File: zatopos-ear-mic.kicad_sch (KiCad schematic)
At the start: 20 parts, among them J2 Conn_01x06_Socket, U1 NJU7043, U2 MCP3002

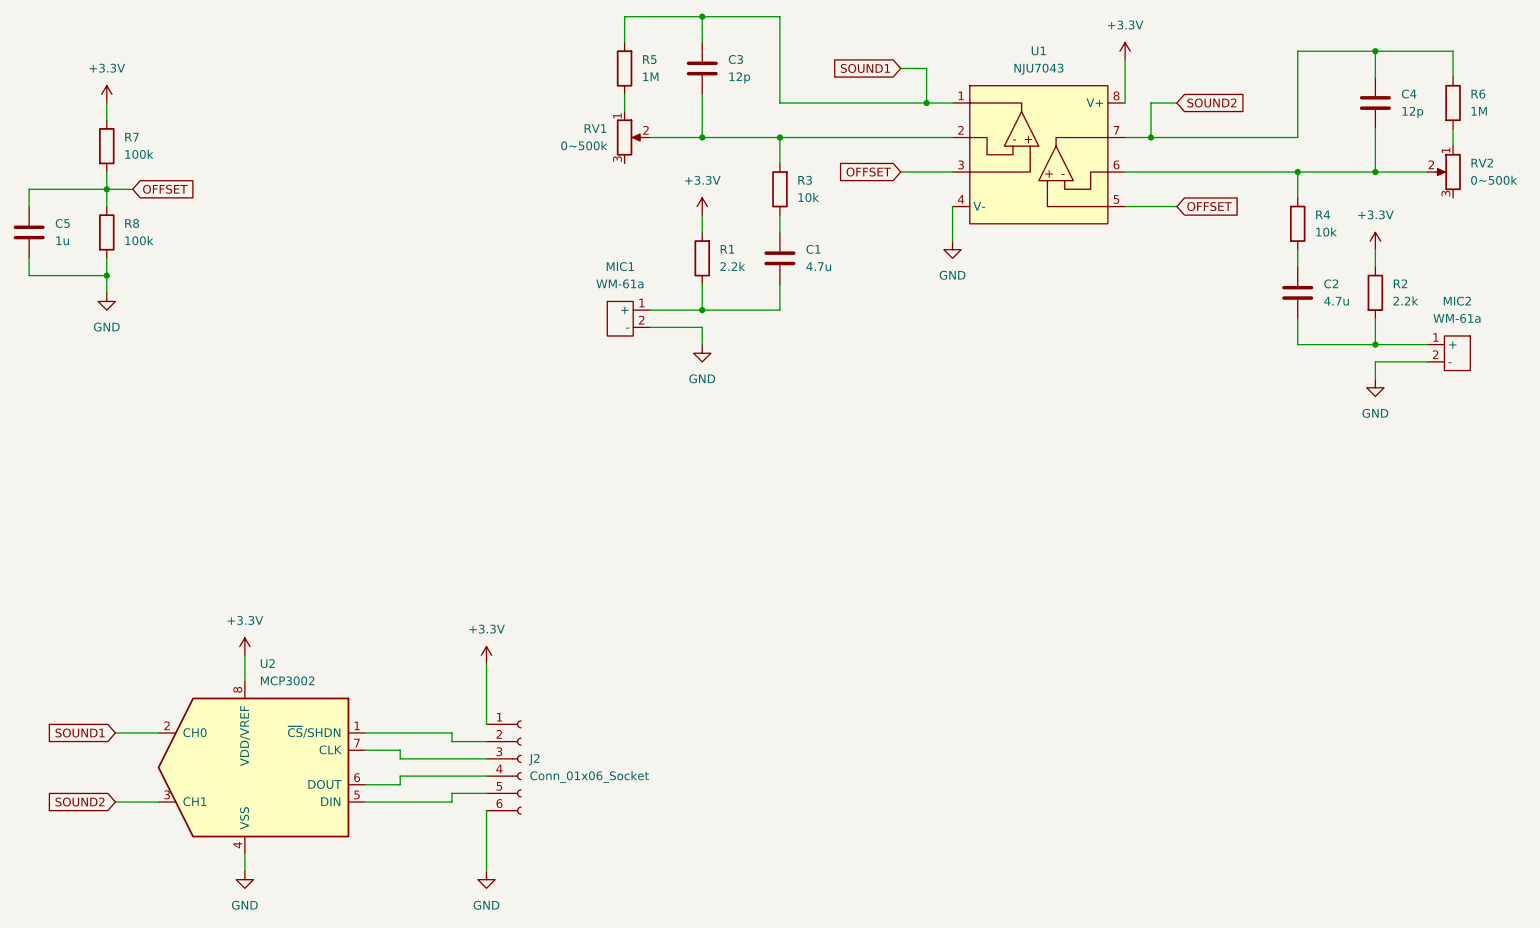
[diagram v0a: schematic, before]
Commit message: Fix ERC errors
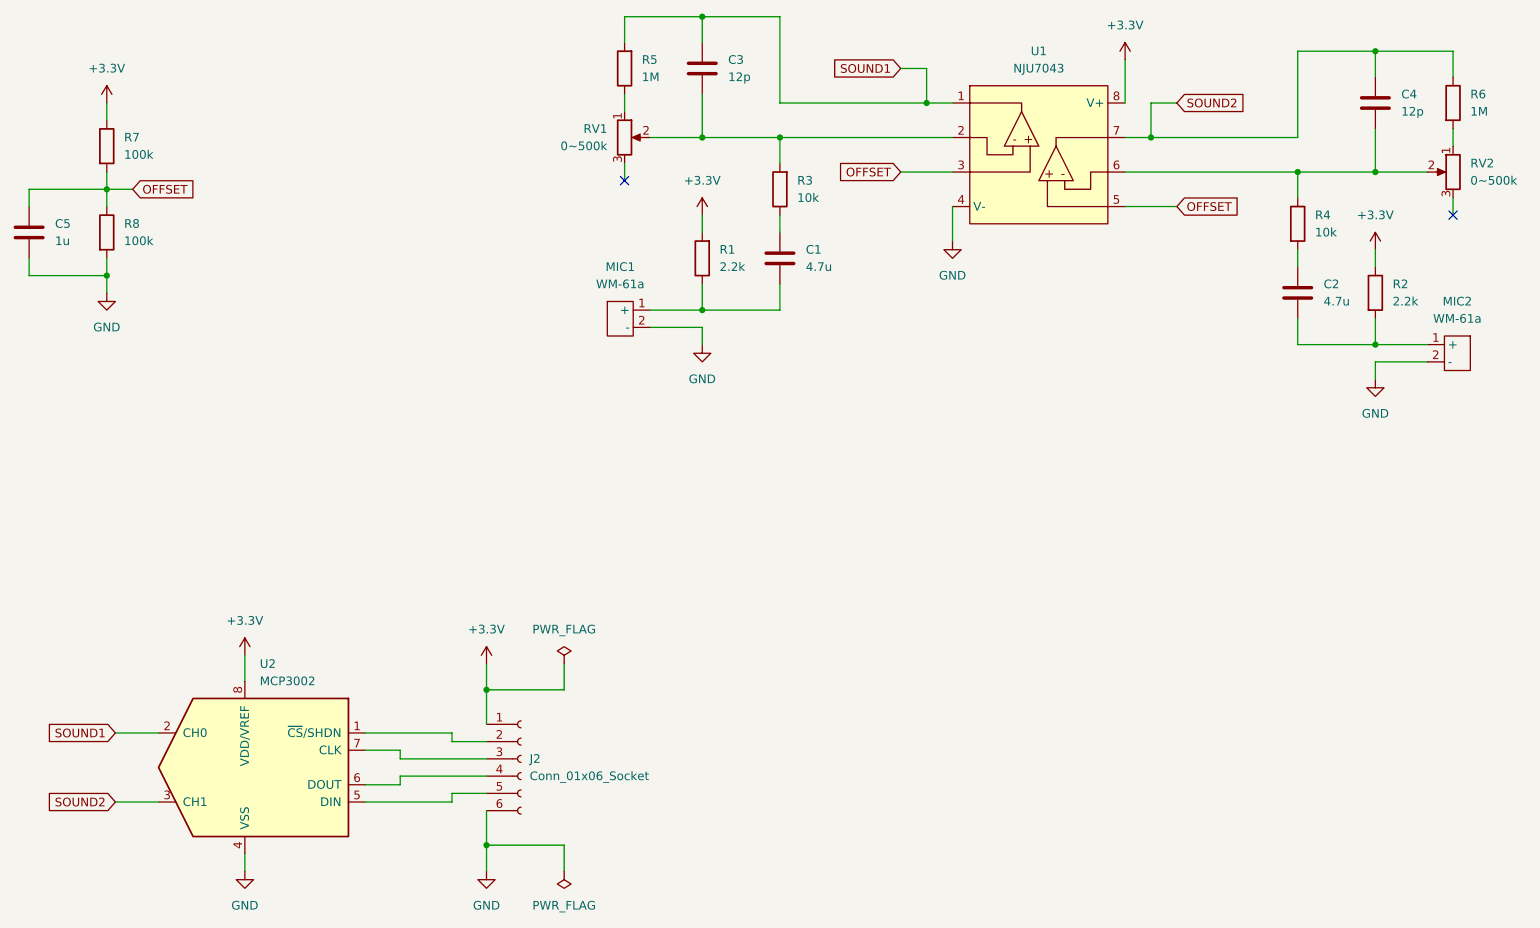
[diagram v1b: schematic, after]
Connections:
- no-connect marks 0 -> 2
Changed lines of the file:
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@@
 	)
 	(junction
+		(at 115.57 138.43)
+		(diameter 0)
+		(color 0 0 0 0)
+	)
+	(junction
 		(at 158.75 57.15)
 		(diameter 0)
@@
 	)
 	(junction
+		(at 115.57 161.29)
+		(diameter 0)
+		(color 0 0 0 0)
+	)
+	(junction
 		(at 180.34 52.07)
 		(diameter 0)
@@
 		(color 0 0 0 0)
 	)
+	(no_connect
+		(at 135.89 63.5)
+	)
+	(no_connect
+		(at 257.81 68.58)
+	)
 	(wire
 		(pts
@@
 	(wire
 		(pts
+			(xy 115.57 161.29) (xy 115.57 165.1)
+		)
+		(stroke
+			(width 0)
+			(type default)
+		)
+	)
+	(wire
+		(pts
 			(xy 102.87 152.4) (xy 102.87 151.13)
 		)
@@
 	(wire
 		(pts
+			(xy 257.81 68.58) (xy 257.81 66.04)
+		)
+		(stroke
+			(width 0)
+			(type default)
+		)
+	)
+	(wire
+		(pts
 			(xy 209.55 45.72) (xy 209.55 52.07)
 		)
@@
 	(wire
 		(pts
+			(xy 127 138.43) (xy 115.57 138.43)
+		)
+		(stroke
+			(width 0)
+			(type default)
+		)
+	)
+	(wire
+		(pts
 			(xy 147.32 39.37) (xy 135.89 39.37)
 		)
@@
 	(wire
 		(pts
-			(xy 115.57 156.21) (xy 115.57 165.1)
+			(xy 115.57 156.21) (xy 115.57 161.29)
 		)
 		(stroke
@@
 	(wire
 		(pts
+			(xy 135.89 63.5) (xy 135.89 60.96)
+		)
+		(stroke
+			(width 0)
+			(type default)
+		)
+	)
+	(wire
+		(pts
 			(xy 246.38 90.17) (xy 246.38 92.71)
 		)
@@
 	(wire
 		(pts
+			(xy 115.57 138.43) (xy 115.57 143.51)
+		)
+		(stroke
+			(width 0)
+			(type default)
+		)
+	)
+	(wire
+		(pts
+			(xy 127 165.1) (xy 127 161.29)
+		)
+		(stroke
+			(width 0)
+			(type default)
+		)
+	)
+	(wire
+		(pts
 			(xy 135.89 43.18) (xy 135.89 39.37)
 		)
@@
 	(wire
 		(pts
-			(xy 115.57 134.62) (xy 115.57 143.51)
+			(xy 127 161.29) (xy 115.57 161.29)
+		)
+		(stroke
+			(width 0)
+			(type default)
+		)
+	)
+	(wire
+		(pts
+			(xy 115.57 134.62) (xy 115.57 138.43)
 		)
 		(stroke
@@
 	(wire
 		(pts
+			(xy 127 134.62) (xy 127 138.43)
+		)
+		(stroke
+			(width 0)
+			(type default)
+		)
+	)
+	(wire
+		(pts
 			(xy 63.5 64.77) (xy 59.69 64.77)
 		)
@@
 					(unit 1)
 				)
+			)
+		)
+	)
+	(symbol
+		(lib_id "power:PWR_FLAG")
+		(at 127 165.1 180)
+		(unit 1)
+		(exclude_from_sim no)
+		(in_bom yes)
+		(on_board yes)
+		(dnp no)
+		(fields_autoplaced yes)
+		(property "Reference" "#FLG02"
+			(at 127 167.005 0)
+			(effects
+				(font
+					(size 1.27 1.27)
+				)
+				(hide yes)
+			)
+		)
+		(property "Value" "PWR_FLAG"
+			(at 127 170.18 0)
+			(effects
+				(font
+					(size 1.27 1.27)
+				)
+			)
+		)
+		(property "Footprint" ""
+			(at 127 165.1 0)
+			(effects
+				(font
+					(size 1.27 1.27)
+				)
+				(hide yes)
+			)
+		)
+		(property "Datasheet" "~"
+			(at 127 165.1 0)
+			(effects
+				(font
+					(size 1.27 1.27)
+				)
+				(hide yes)
+			)
+		)
+		(property "Description" "Special symbol for telling ERC where power comes from"
+			(at 127 165.1 0)
+			(effects
+				(font
+					(size 1.27 1.27)
+				)
+				(hide yes)
+			)
+		)
+		(pin "1"
+		)
+		(instances
+			(project ""
+				(path "/e6ed543b-f5df-4af1-90bb-8e380cee6410"
+					(reference "#FLG02")
+					(unit 1)
+				)
+			)
+		)
+	)
+	(symbol
+		(lib_id "power:PWR_FLAG")
+		(at 127 134.62 0)
+		(unit 1)
+		(exclude_from_sim no)
+		(in_bom yes)
+		(on_board yes)
+		(dnp no)
+		(fields_autoplaced yes)
+		(property "Reference" "#FLG01"
+			(at 127 132.715 0)
+			(effects
+				(font
+					(size 1.27 1.27)
+				)
+				(hide yes)
+			)
+		)
+		(property "Value" "PWR_FLAG"
+			(at 127 129.54 0)
+			(effects
+				(font
+					(size 1.27 1.27)
+				)
+			)
+		)
+		(property "Footprint" ""
+			(at 127 134.62 0)
+			(effects
+				(font
+					(size 1.27 1.27)
+				)
+				(hide yes)
+			)
+		)
+		(property "Datasheet" "~"
+			(at 127 134.62 0)
+			(effects
+				(font
+					(size 1.27 1.27)
+				)
+				(hide yes)
+			)
+		)
+		(property "Description" "Special symbol for telling ERC where power comes from"
+			(at 127 134.62 0)
+			(effects
+				(font
+					(size 1.27 1.27)
+				)
+				(hide yes)
+			)
+		)
+		(pin "1"
+		)
+		(instances
+			(project ""
+				(path "/e6ed543b-f5df-4af1-90bb-8e380cee6410"
+					(reference "#FLG01")
+					(unit 1)
+				)

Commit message: Assign footprints
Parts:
- C1, C2, C3, C4, C5: footprint (none) -> Capacitor_SMD:C_1206_3216Metric
- J2: footprint (none) -> Connector_JST:JST_XH_B6B-XH-A_1x06_P2.50mm_Vertical
- MIC1, MIC2: footprint (none) -> Mic:WM-61a
- R1, R2, R3, R4, R5, R6, R7, R8: footprint (none) -> Resistor_SMD:R_1206_3216Metric
- RV1, RV2: footprint (none) -> Mic:GF063P
- U1, U2: footprint (none) -> Package_DIP:DIP-8_W7.62mm_Socket
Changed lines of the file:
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@@
 			)
 		)
-		(property "Footprint" ""
+		(property "Footprint" "Resistor_SMD:R_1206_3216Metric"
 			(at 160.528 64.77 90)
 			(effects
@@
 			)
 		)
-		(property "Footprint" ""
+		(property "Footprint" "Mic:WM-61a"
 			(at 135.89 88.392 0)
 			(effects
@@
 			)
 		)
-		(property "Footprint" ""
+		(property "Footprint" "Capacitor_SMD:C_1206_3216Metric"
 			(at 148.2852 50.8 0)
 			(effects
@@
 			)
 		)
-		(property "Footprint" ""
+		(property "Footprint" "Mic:WM-61a"
 			(at 257.81 93.472 0)
 			(effects
@@
 			)
 		)
-		(property "Footprint" ""
+		(property "Footprint" "Mic:GF063P"
 			(at 257.81 62.23 0)
 			(effects
@@
 			)
 		)
-		(property "Footprint" ""
+		(property "Footprint" "Resistor_SMD:R_1206_3216Metric"
 			(at 149.098 74.93 90)
 			(effects
@@
 			)
 		)
-		(property "Footprint" ""
+		(property "Footprint" "Resistor_SMD:R_1206_3216Metric"
 			(at 244.602 80.01 90)
 			(effects
@@
 			)
 		)
-		(property "Footprint" ""
+		(property "Footprint" "Resistor_SMD:R_1206_3216Metric"
 			(at 256.032 52.07 90)
 			(effects
@@
 			)
 		)
-		(property "Footprint" ""
+		(property "Footprint" "Resistor_SMD:R_1206_3216Metric"
 			(at 57.912 58.42 90)
 			(effects
@@
 			)
 		)
-		(property "Footprint" ""
+		(property "Footprint" "Capacitor_SMD:C_1206_3216Metric"
 			(at 159.7152 78.74 0)
 			(effects
@@
 			)
 		)
-		(property "Footprint" ""
+		(property "Footprint" "Package_DIP:DIP-8_W7.62mm_Socket"
 			(at 80.01 152.4 0)
 			(effects
@@
 			)
 		)
-		(property "Footprint" ""
+		(property "Footprint" "Capacitor_SMD:C_1206_3216Metric"
 			(at 247.3452 55.88 0)
 			(effects
@@
 			)
 		)
-		(property "Footprint" ""
+		(property "Footprint" "Capacitor_SMD:C_1206_3216Metric"
 			(at 235.9152 83.82 0)
 			(effects
@@
 			)
 		)
-		(property "Footprint" ""
+		(property "Footprint" "Package_DIP:DIP-8_W7.62mm_Socket"
 			(at 196.85 59.69 0)
 			(effects
@@
 			)
 		)
-		(property "Footprint" ""
+		(property "Footprint" "Resistor_SMD:R_1206_3216Metric"
 			(at 137.668 46.99 90)
 			(effects
@@
 			)
 		)
-		(property "Footprint" ""
+		(property "Footprint" "Capacitor_SMD:C_1206_3216Metric"
 			(at 49.2252 74.93 0)
 			(effects
@@
 		(on_board yes)
 		(dnp no)
-		(fields_autoplaced yes)
 		(property "Reference" "J2"
 			(at 121.92 148.5899 0)
@@
 			)
 		)
-		(property "Footprint" ""
-			(at 120.65 148.59 0)
+		(property "Footprint" "Connector_JST:JST_XH_B6B-XH-A_1x06_P2.50mm_Vertical"
+			(at 150.114 156.464 0)
 			(effects
 				(font
@@
 			)
 		)
-		(property "Footprint" ""
+		(property "Footprint" "Mic:GF063P"
 			(at 135.89 57.15 0)
 			(effects
@@
 			)
 		)
-		(property "Footprint" ""
+		(property "Footprint" "Resistor_SMD:R_1206_3216Metric"
 			(at 57.912 71.12 90)
 			(effects
@@
 			)
 		)
-		(property "Footprint" ""
+		(property "Footprint" "Resistor_SMD:R_1206_3216Metric"
 			(at 233.172 69.85 90)
 			(effects

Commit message: Write caption
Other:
- company: (none) -> Shinagawa Kazemaru
- title: (none) -> zatopos-ear-mic
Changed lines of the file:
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@@
 	(generator_version "8.0")
 	(paper "A4")
+	(title_block
+		(title "zatopos-ear-mic")
+		(date "2024-10-30")
+		(company "Shinagawa Kazemaru")
+		(comment 1 "Two microphone & one A/D converter")
+		(comment 2 "For zatopos-ear")
+	)
 	(junction
 		(at 147.32 39.37)

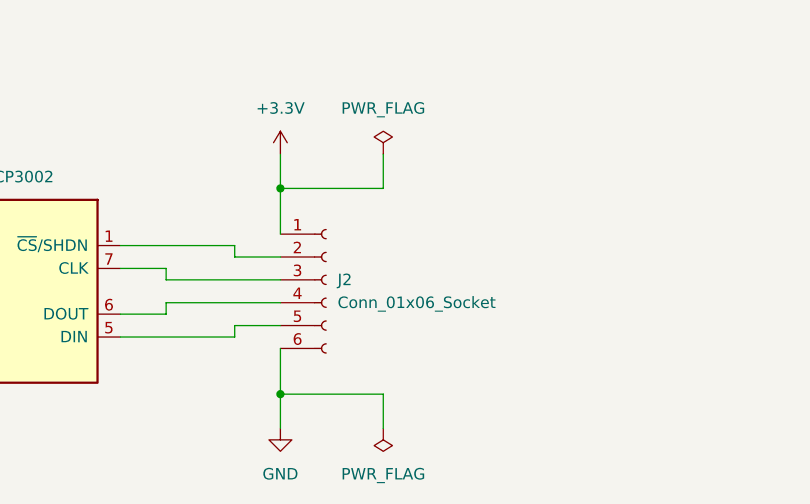
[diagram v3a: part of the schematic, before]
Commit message: Place footprints
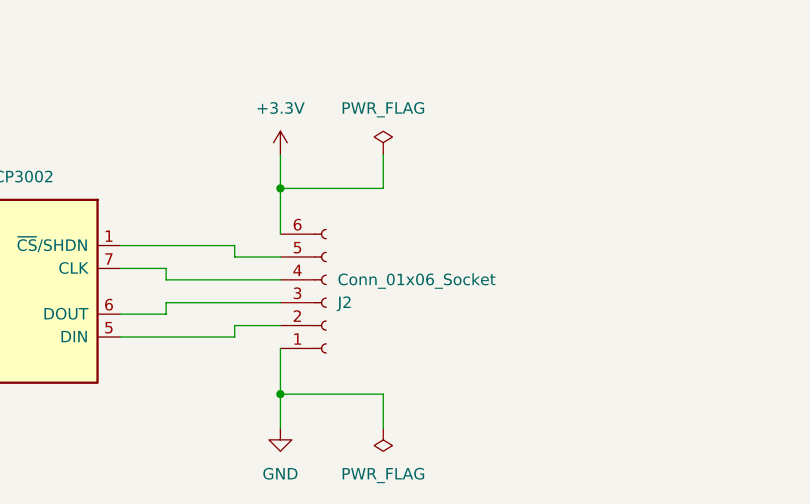
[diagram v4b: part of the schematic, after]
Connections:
- net +3.3V: now also J2.6 (Pin_6); no longer J2.1 (Pin_1)
- net GND: now also J2.1 (Pin_1); no longer J2.6 (Pin_6)
- net at U2.1 (~{CS}/SHDN): now also J2.5 (Pin_5); no longer J2.2 (Pin_2)
- net at U2.5 (DIN): now also J2.2 (Pin_2); no longer J2.5 (Pin_5)
- net at U2.6 (DOUT): now also J2.3 (Pin_3); no longer J2.4 (Pin_4)
- net at U2.7 (CLK): now also J2.4 (Pin_4); no longer J2.3 (Pin_3)
